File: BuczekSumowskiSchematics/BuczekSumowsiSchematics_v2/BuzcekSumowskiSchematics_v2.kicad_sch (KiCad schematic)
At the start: 0 parts

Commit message: basic stm32 connection (without source)
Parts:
- added C?: 10u, symbol Device:C
- added C? (x5): 100n, symbol Device:C
- added C? (x2): 1u, symbol Device:C
- added C?: 10n, symbol Device:C
- added FB?: 120R, symbol Device:FerriteBead
- added R?: 10k, symbol Device:R
- added SW?: SW_SPDT, symbol Switch:SW_SPDT
- added U?: STM32F446RET6U, Package_QFP:LQFP-64_10x10mm_P0.5mm, symbol MCU_ST_STM32F4:STM32F446RETx
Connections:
- new net +3.3V: C?.1, C?.1, C?.1, C?.1, C?.1, C?.1, FB?.2, SW?.3 (C), U?.1 (VBAT), U?.19 (VDD), U?.32 (VDD), U?.48 (VDD), U?.64 (VDD)
- new net +3.3VA: C?.1, C?.1, FB?.1, U?.13 (VDDA)
- new net BOOT0: R?.2, U?.60 (BOOT0)
- new net GND: C?.2, C?.2, C?.2, C?.2, C?.2, C?.2, C?.2, C?.2, C?.2, SW?.1 (A), U?.12 (VSSA), U?.18 (VSS), U?.31 (VSS), U?.47 (VSS), U?.63 (VSS)
- new net NRST: C?.1, U?.7 (NRST)
- new net SW_BOOT0: R?.1, SW?.2 (B)

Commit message: schemtics progress
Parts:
- removed C?: 10u, symbol Device:C
- removed C? (x4): 100n, symbol Device:C
- added C? (x2): 10p, symbol Device:C
- added C? (x11): 100n, Capacitor_SMD:C_0805_2012Metric_Pad1.18x1.45mm_HandSolder, symbol Device:C
- added C? (x4): 22u, Capacitor_SMD:C_0805_2012Metric_Pad1.18x1.45mm_HandSolder, symbol Device:C
- added C? (x3): 10u, Capacitor_Tantalum_SMD:CP_EIA-3216-18_Kemet-A_Pad1.58x1.35mm_HandSolder, symbol Device:C_Polarized
- added C?: 1u, Capacitor_Tantalum_SMD:CP_EIA-3216-18_Kemet-A_Pad1.58x1.35mm_HandSolder, symbol Device:C_Polarized
- added J?: USB_B_Micro, symbol Connector:USB_B_Micro
- added J?: NXW-02, Connector_Molex:Molex_Micro-Latch_53253-0270_1x02_P2.00mm_Vertical, symbol Connector_Generic:Conn_01x02
- added J?: Conn_01x04_Male, symbol Connector:Conn_01x04_Male
- added L? (x2): XAL4020-222MEC, Inductor_SMD:L_Coilcraft_XxL4040, symbol SamacSys_Parts:XAL4020-222MEC
- added R? (x4): R, Resistor_SMD:R_0805_2012Metric_Pad1.20x1.40mm_HandSolder, symbol Device:R
- added R?: 1k5, symbol Device:R
- added R? (x2): 100k, Resistor_SMD:R_0805_2012Metric_Pad1.20x1.40mm_HandSolder, symbol Device:R
- added R? (x2): 25k5, Resistor_SMD:R_0805_2012Metric_Pad1.20x1.40mm_HandSolder, symbol Device:R
- added ST? (x2): TPS565242DRLR, Package_TO_SOT_SMD:SOT-563, symbol SamacSys_Parts:TPS565242DRLR
- added Y?: 16MHz, symbol Device:Crystal_GND24
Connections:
- net +3.3V: now also J?.1 (Pin_1), R?.1
- net GND: now also C?.2, C?.2, C?.2, C?.2, C?.2, C?.2, C?.2, C?.2, C?.2, C?.2, C?.2, C?.2, C?.2, C?.2, C?.2, C?.2, C?.2, C?.2, C?.2, C?.2, C?.2, J?.2 (Pin_2), J?.4 (Pin_4), J?.5 (GND), R?.1, R?.1, R?.1, R?.1, ST?.3 (GND), ST?.3 (GND), ST?.4 (AGND), ST?.4 (AGND), Y?.2, Y?.4
- net USB_D-: now reaches U?.44 (PA11)
- net USB_D-: now also J?.2 (D-)
- net USB_D+: now reaches U?.45 (PA12)
- net USB_D+: now also J?.3 (D+), R?.2
- net SWDIO: now reaches U?.46 (PA13)
- net SWDIO: now also J?.2 (Pin_2)
- net SWCLK: now reaches U?.49 (PA14)
- net SWCLK: now also J?.3 (Pin_3)
- net HSE_IN: now reaches U?.5 (PH0)
- net HSE_IN: now also C?.1, Y?.1
- net HSE_OUT: now reaches U?.6 (PH1)
- net HSE_OUT: now also C?.1, Y?.3
- new net: L?.1, ST?.2 (SW) (x2)
- new net: R?.2, R?.2, ST?.5 (EN)
- new net +3V3: C?.1, C?.1, C?.1, C?.1, C?.1, C?.1, C?.1, C?.1, C?.1, C?.1, C?.1, C?.1, L?.2, R?.2
- new net +5V: C?.1, C?.1, L?.2, R?.1, R?.2, ST?.1 (VIN)
- new net +BATT: C?.1, C?.1, C?.1, C?.1, C?.1, J?.1 (Pin_1), R?.1, ST?.1 (VIN)
- new net FB3V3: R?.1, R?.2, ST?.6 (FB)
- new net FB5V: R?.1, R?.2, ST?.6 (FB)
- new net Switch: R?.2, R?.2, ST?.5 (EN)
- new net VBUS: J?.1 (VBUS)
- no-connect marks 0 -> 2
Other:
- moved on the sheet: C?, FB?, R?, SW?, U?

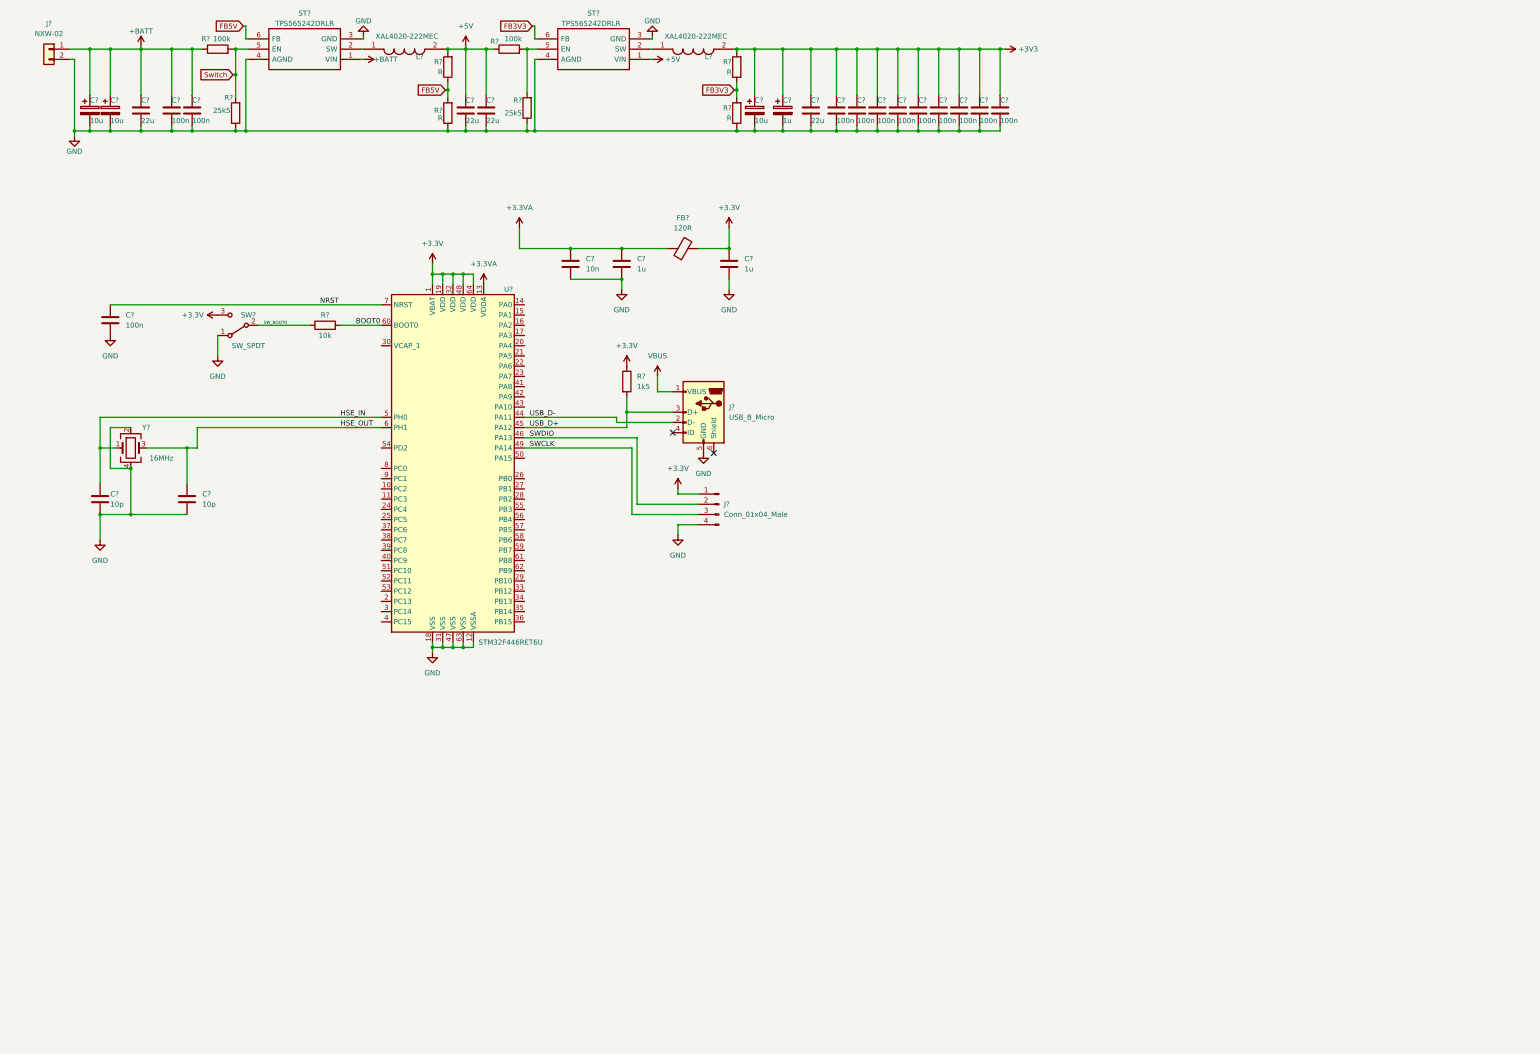
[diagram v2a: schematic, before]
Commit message: schmetics updates
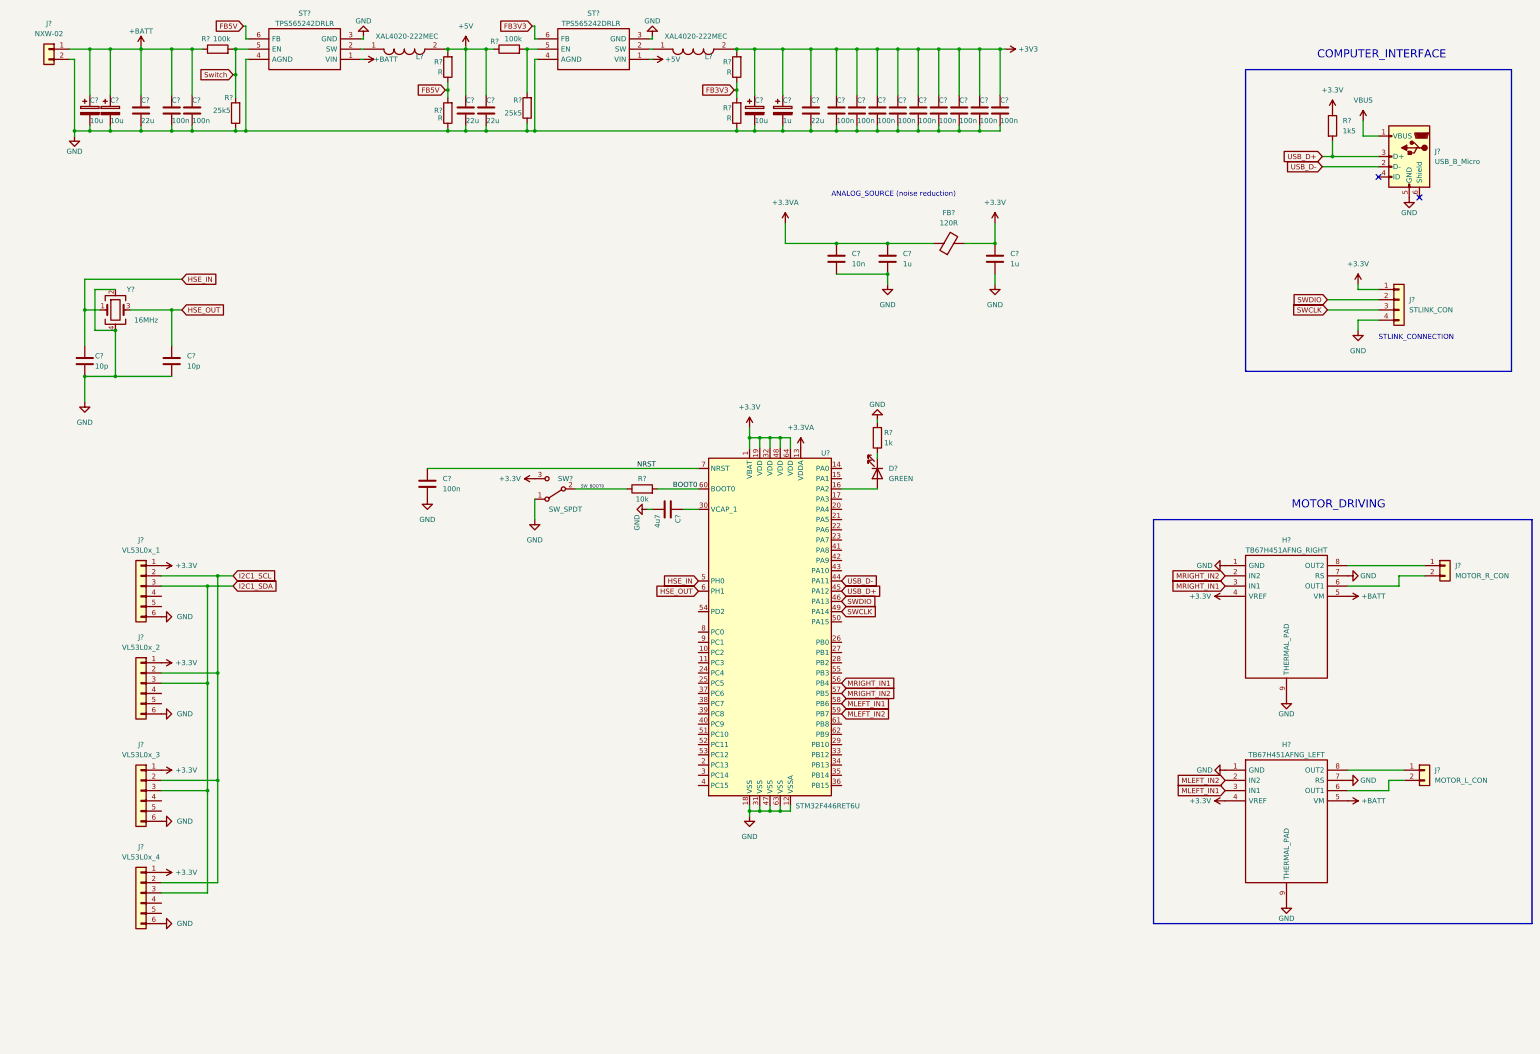
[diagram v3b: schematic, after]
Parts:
- removed J?: Conn_01x04_Male, symbol Connector:Conn_01x04_Male
- added C?: 4u7, Capacitor_SMD:C_0805_2012Metric, symbol Device:C
- added D?: GREEN, LED_SMD:LED_1206_3216Metric_Pad1.42x1.75mm_HandSolder, symbol Device:LED
- added H?: TB67H451AFNG_LEFT, Package_SO:HSOP-8-1EP_3.9x4.9mm_P1.27mm_EP2.41x3.1mm_ThermalVias, symbol SamacSys_Parts:TB67H451AFNG,EL
- added H?: TB67H451AFNG_RIGHT, Package_SO:HSOP-8-1EP_3.9x4.9mm_P1.27mm_EP2.41x3.1mm_ThermalVias, symbol SamacSys_Parts:TB67H451AFNG,EL
- added J?: VL53L0x_4, symbol Connector_Generic:Conn_01x06
- added J?: VL53L0x_1, symbol Connector_Generic:Conn_01x06
- added J?: VL53L0x_3, symbol Connector_Generic:Conn_01x06
- added J?: MOTOR_R_CON, symbol Connector_Generic:Conn_01x02
- added J?: STLINK_CON, symbol Connector_Generic:Conn_01x04
- added J?: MOTOR_L_CON, symbol Connector_Generic:Conn_01x02
- added J?: VL53L0x_2, symbol Connector_Generic:Conn_01x06
- added R?: 1k, Resistor_SMD:R_0805_2012Metric_Pad1.20x1.40mm_HandSolder, symbol Device:R
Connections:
- net +3.3V: now also H?.4 (VREF), H?.4 (VREF), J?.1 (Pin_1), J?.1 (Pin_1), J?.1 (Pin_1), J?.1 (Pin_1), J?.1 (Pin_1)
- net +BATT: now also H?.5 (VM), H?.5 (VM)
- net GND: now also C?.2, H?.1 (GND), H?.1 (GND), H?.7 (RS), H?.7 (RS), H?.9 (THERMAL_PAD), H?.9 (THERMAL_PAD), J?.4 (Pin_4), J?.6 (Pin_6), J?.6 (Pin_6), J?.6 (Pin_6), J?.6 (Pin_6), R?.2
- net SWCLK: now also J?.3 (Pin_3)
- net SWDIO: now also J?.2 (Pin_2)
- net at U?.16 (PA2): now also D?.2 (A)
- net at U?.30 (VCAP_1): now also C?.1
- net MRIGHT_IN1: now reaches U?.56 (PB4)
- net MRIGHT_IN1: now also H?.3 (IN1)
- net MRIGHT_IN2: now reaches U?.57 (PB5)
- net MRIGHT_IN2: now also H?.2 (IN2)
- net MLEFT_IN1: now reaches U?.58 (PB6)
- net MLEFT_IN1: now also H?.3 (IN1)
- net MLEFT_IN2: now reaches U?.59 (PB7)
- net MLEFT_IN2: now also H?.2 (IN2)
- new net: D?.1 (K), R?.1
- new net: H?.6 (OUT1), J?.2 (Pin_2) (x2)
- new net: H?.8 (OUT2), J?.1 (Pin_1) (x2)
- new net I2C1_SCL: J?.2 (Pin_2), J?.2 (Pin_2), J?.2 (Pin_2), J?.2 (Pin_2)
- new net I2C1_SDA: J?.3 (Pin_3), J?.3 (Pin_3), J?.3 (Pin_3), J?.3 (Pin_3)
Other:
- note added: "ANALOG_SOURCE (noise reduction)"
- note added: "COMPUTER_INTERFACE"
- note added: "MOTOR_DRIVING"
- note added: "STLINK_CONNECTION"
- moved on the sheet: C?, FB?, J?, R?, SW?, U?, Y?

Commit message: schematic sensors added
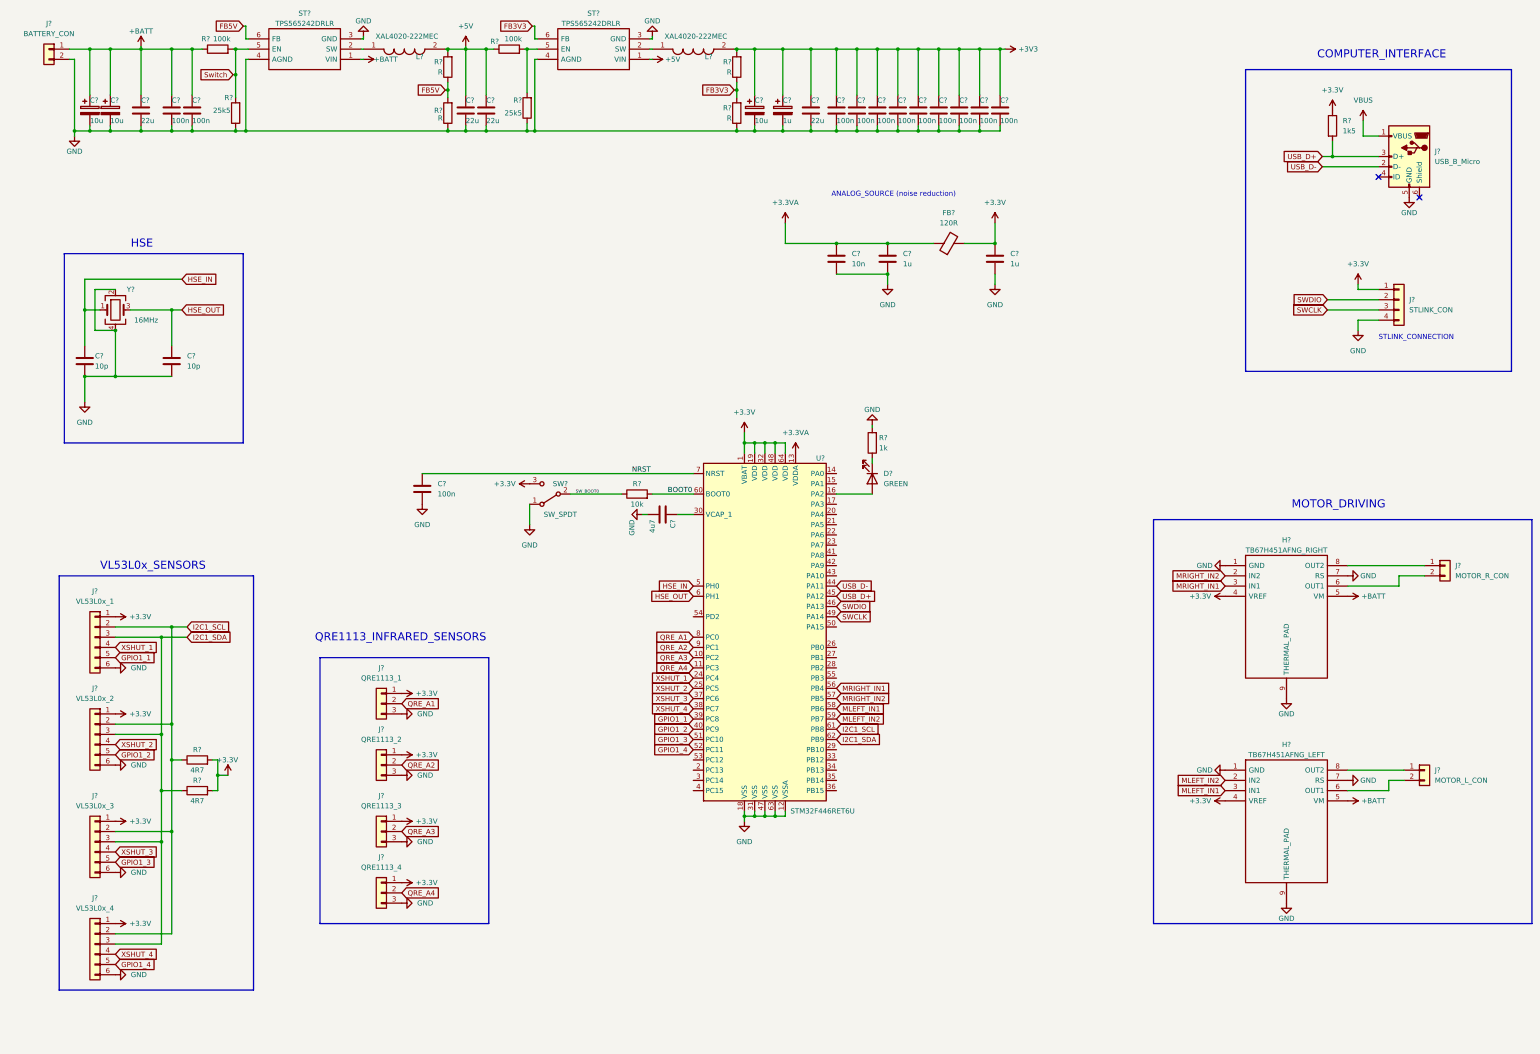
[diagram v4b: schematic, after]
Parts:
- added J?: QRE1113_4, symbol Connector_Generic:Conn_01x03
- added J?: QRE1113_2, symbol Connector_Generic:Conn_01x03
- added J?: QRE1113_1, symbol Connector_Generic:Conn_01x03
- added J?: QRE1113_3, symbol Connector_Generic:Conn_01x03
- added R? (x2): 4R7, symbol Device:R
- J?: value NXW-02 -> BATTERY_CON
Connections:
- net +3.3V: now also J?.1 (Pin_1), J?.1 (Pin_1), J?.1 (Pin_1), J?.1 (Pin_1), R?.2, R?.2
- net GND: now also J?.3 (Pin_3), J?.3 (Pin_3), J?.3 (Pin_3), J?.3 (Pin_3)
- net I2C1_SCL: now also U?.61 (PB8), R?.1
- net I2C1_SDA: now also U?.62 (PB9), R?.1
- net XSHUT_4: now reaches J?.4 (Pin_4)
- net XSHUT_4: now also U?.38 (PC7)
- net GPIO1_4: now reaches J?.5 (Pin_5)
- net GPIO1_4: now also U?.52 (PC11)
- net XSHUT_1: now reaches J?.4 (Pin_4)
- net XSHUT_1: now also U?.24 (PC4)
- net GPIO1_1: now reaches J?.5 (Pin_5)
- net GPIO1_1: now also U?.39 (PC8)
- net XSHUT_3: now reaches J?.4 (Pin_4)
- net XSHUT_3: now also U?.37 (PC6)
- net GPIO1_3: now reaches J?.5 (Pin_5)
- net GPIO1_3: now also U?.51 (PC10)
- net QRE_A3: now reaches U?.10 (PC2)
- net QRE_A3: now also J?.2 (Pin_2)
- net QRE_A4: now reaches U?.11 (PC3)
- net QRE_A4: now also J?.2 (Pin_2)
- net XSHUT_2: now reaches U?.25 (PC5)
- net XSHUT_2: now also J?.4 (Pin_4)
- net GPIO1_2: now reaches U?.40 (PC9)
- net GPIO1_2: now also J?.5 (Pin_5)
- net QRE_A1: now reaches U?.8 (PC0)
- net QRE_A1: now also J?.2 (Pin_2)
- net QRE_A2: now reaches U?.9 (PC1)
- net QRE_A2: now also J?.2 (Pin_2)
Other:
- note added: "HSE"
- note added: "QRE1113_INFRARED_SENSORS"
- note added: "VL53L0x_SENSORS"
- moved on the sheet: C?, D?, J?, R?, SW?, U?

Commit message: almost ready for check (maybe diff h-bridge?)
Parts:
- added H? (x4): MountingHole_Pad, MountingHole:MountingHole_3.2mm_M3_Pad_Via, symbol Mechanical:MountingHole_Pad
- added SW?: POWER_SW, symbol Switch:SW_SPDT
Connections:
- net GND: now also H?.1, H?.1, H?.1, H?.1, SW?.1 (A)
- net Switch renamed Power_sw
- net Power_sw: now also SW?.2 (B)
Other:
- note added: "POWER_SOURCE"
- moved on the sheet: C?, FB?, J?, L?, R?, ST?, Y?

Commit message: better orginized
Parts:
- removed C?: 100n, symbol Device:C
- added C?: 100n, symbol Device:C
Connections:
- net GND: now also C?.2
- net BOOT0: no longer names the net of R?.2, U?.60 (BOOT0)
- net NRST: no longer names the net of U?.7 (NRST)
- net NRST: now also C?.1
- net SW_BOOT0: no longer names the net of R?.1, SW?.2 (B)
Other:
- moved on the sheet: C?, J?, R?, SW?, Y?
